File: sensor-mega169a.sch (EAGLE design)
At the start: 55 parts, among them IC3 ATmega169PA, K1 SP6029TOP, M1 NRF24L01P-M, M2 DHT22, Q1 IRLML2502, Q2 IRLML2502, Q3 IRLML6402, U1 MCP1640C, U2 MCP604-I/ST

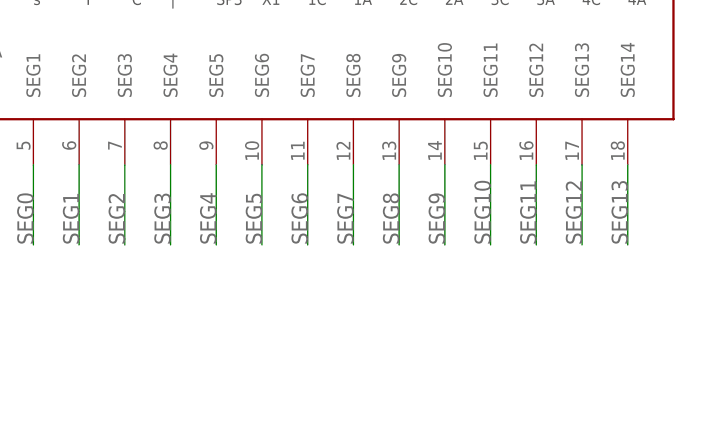
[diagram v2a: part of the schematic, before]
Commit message: cc-by-sa license
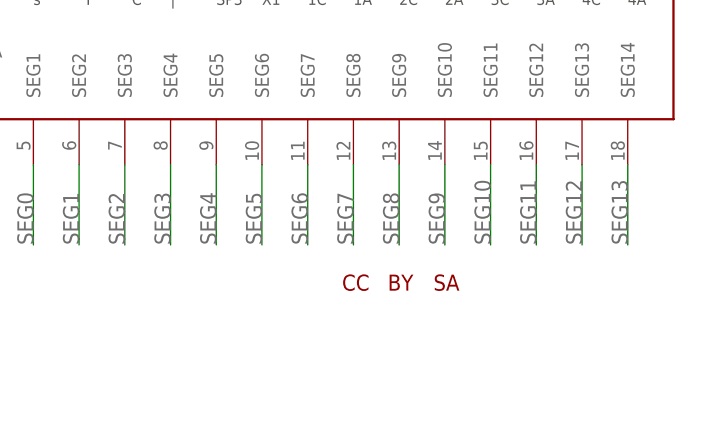
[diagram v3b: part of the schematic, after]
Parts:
- added U$1: CC-TPLACE-HALF, creative-commons:CC-TPLACE-HALF
- added U$3: BY-TPLACE-HS, creative-commons:BY-TPLACE-HS
- added U$4: SA-TPLACE-HALF, creative-commons:SA-TPLACE-HALF

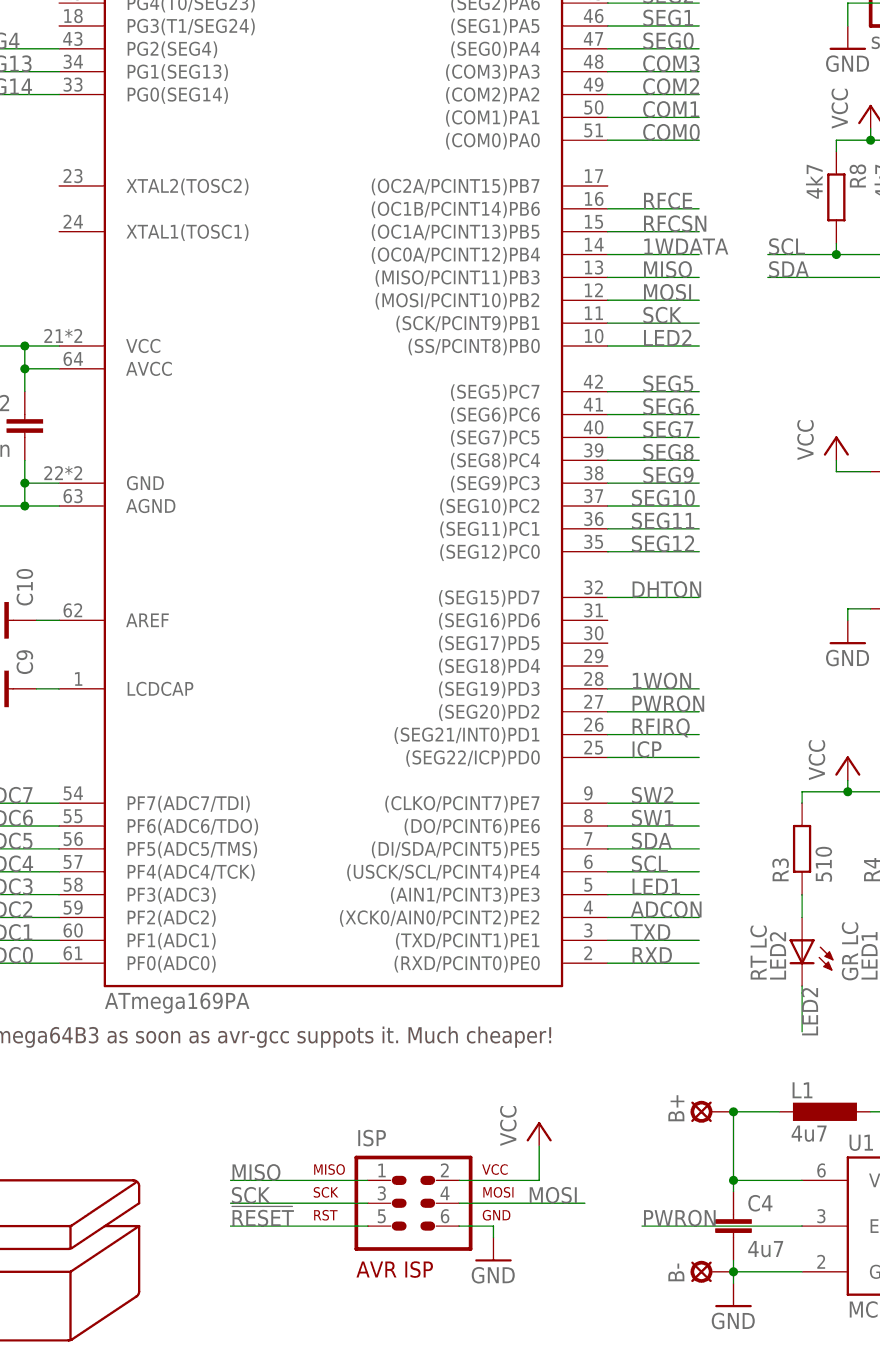
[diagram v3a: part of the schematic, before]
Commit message: added jumper for spi slave extensions on isp header
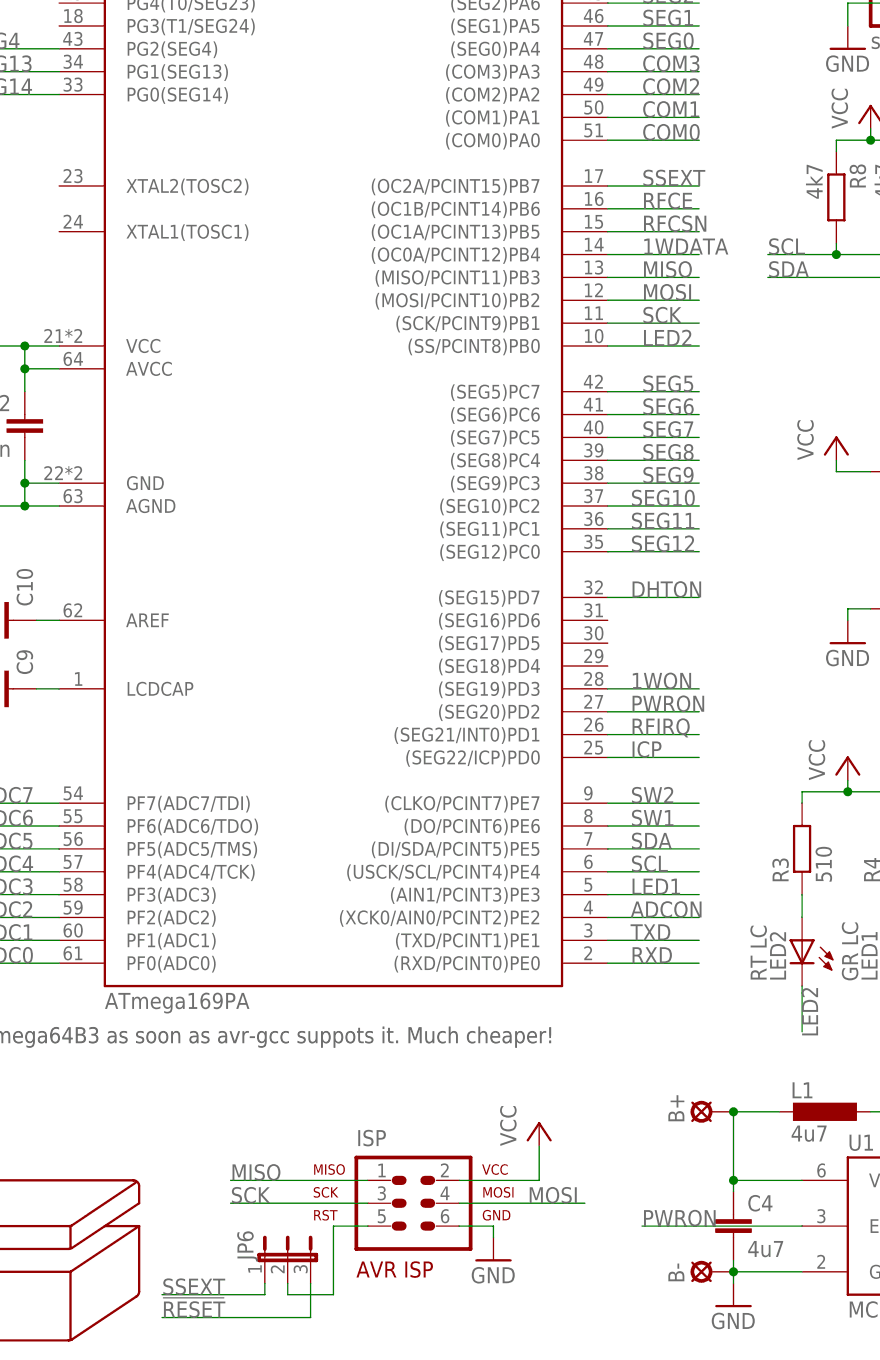
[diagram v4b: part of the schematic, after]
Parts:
- added JP6: (no value), jumper:JP2E
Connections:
- new net N$6: ISP.5, JP6.2
- new net SSEXT: IC3.(OC2A/PCINT15)PB7, JP6.1
- net !RESET: now also JP6.3; no longer ISP.5
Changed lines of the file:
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@@
 <setting verticaltext="up"/>
 </settings>
-<grid distance="0.1" unitdist="inch" unit="mm" style="lines" multiple="1" display="yes" altdistance="0.01" altunitdist="inch" altunit="mm"/>
+<grid distance="1.27" unitdist="mm" unit="mm" style="lines" multiple="1" display="yes" altdistance="635" altunitdist="mic" altunit="mic"/>
 <layers>
-<layer number="1" name="Top" color="4" fill="1" visible="yes" active="no"/>
-<layer number="2" name="Route2" color="1" fill="3" visible="yes" active="no"/>
-<layer number="3" name="Route3" color="4" fill="3" visible="yes" active="no"/>
-<layer number="4" name="Route4" color="1" fill="4" visible="yes" active="no"/>
-<layer number="5" name="Route5" color="4" fill="4" visible="yes" active="no"/>
-<layer number="6" name="Route6" color="1" fill="8" visible="yes" active="no"/>
-<layer number="7" name="Route7" color="4" fill="8" visible="yes" active="no"/>
-<layer number="8" name="Route8" color="1" fill="2" visible="yes" active="no"/>
-<layer number="9" name="Route9" color="4" fill="2" visible="yes" active="no"/>
-<layer number="10" name="Route10" color="1" fill="7" visible="yes" active="no"/>
-<layer number="11" name="Route11" color="4" fill="7" visible="yes" active="no"/>
-<layer number="12" name="Route12" color="1" fill="5" visible="yes" active="no"/>
-<layer number="13" name="Route13" color="4" fill="5" visible="yes" active="no"/>
-<layer number="14" name="Route14" color="1" fill="6" visible="yes" active="no"/>
-<layer number="15" name="Route15" color="4" fill="6" visible="yes" active="no"/>
-<layer number="16" name="Bottom" color="1" fill="1" visible="yes" active="no"/>
-<layer number="17" name="Pads" color="2" fill="1" visible="yes" active="no"/>
-<layer number="18" name="Vias" color="2" fill="1" visible="yes" active="no"/>
-<layer number="19" name="Unrouted" color="6" fill="1" visible="yes" active="no"/>
-<layer number="20" name="Dimension" color="15" fill="1" visible="yes" active="no"/>
-<layer number="21" name="tPlace" color="7" fill="1" visible="yes" active="no"/>
-<layer number="22" name="bPlace" color="7" fill="1" visible="yes" active="no"/>
-<layer number="23" name="tOrigins" color="15" fill="1" visible="yes" active="no"/>
-<layer number="24" name="bOrigins" color="15" fill="1" visible="yes" active="no"/>
-<layer number="25" name="tNames" color="7" fill="1" visible="yes" active="no"/>
-<layer number="26" name="bNames" color="7" fill="1" visible="yes" active="no"/>
-<layer number="27" name="tValues" color="7" fill="1" visible="yes" active="no"/>
-<layer number="28" name="bValues" color="7" fill="1" visible="yes" active="no"/>
+<layer number="1" name="Top" color="4" fill="1" visible="no" active="no"/>
+<layer number="2" name="Route2" color="1" fill="3" visible="no" active="no"/>
+<layer number="3" name="Route3" color="4" fill="3" visible="no" active="no"/>
+<layer number="4" name="Route4" color="1" fill="4" visible="no" active="no"/>
+<layer number="5" name="Route5" color="4" fill="4" visible="no" active="no"/>
+<layer number="6" name="Route6" color="1" fill="8" visible="no" active="no"/>
+<layer number="7" name="Route7" color="4" fill="8" visible="no" active="no"/>
+<layer number="8" name="Route8" color="1" fill="2" visible="no" active="no"/>
+<layer number="9" name="Route9" color="4" fill="2" visible="no" active="no"/>
+<layer number="10" name="Route10" color="1" fill="7" visible="no" active="no"/>
+<layer number="11" name="Route11" color="4" fill="7" visible="no" active="no"/>
+<layer number="12" name="Route12" color="1" fill="5" visible="no" active="no"/>
+<layer number="13" name="Route13" color="4" fill="5" visible="no" active="no"/>
+<layer number="14" name="Route14" color="1" fill="6" visible="no" active="no"/>
+<layer number="15" name="Route15" color="4" fill="6" visible="no" active="no"/>
+<layer number="16" name="Bottom" color="1" fill="1" visible="no" active="no"/>
+<layer number="17" name="Pads" color="2" fill="1" visible="no" active="no"/>
+<layer number="18" name="Vias" color="2" fill="1" visible="no" active="no"/>
+<layer number="19" name="Unrouted" color="6" fill="1" visible="no" active="no"/>
+<layer number="20" name="Dimension" color="15" fill="1" visible="no" active="no"/>
+<layer number="21" name="tPlace" color="7" fill="1" visible="no" active="no"/>
+<layer number="22" name="bPlace" color="7" fill="1" visible="no" active="no"/>
+<layer number="23" name="tOrigins" color="15" fill="1" visible="no" active="no"/>
+<layer number="24" name="bOrigins" color="15" fill="1" visible="no" active="no"/>
+<layer number="25" name="tNames" color="7" fill="1" visible="no" active="no"/>
+<layer number="26" name="bNames" color="7" fill="1" visible="no" active="no"/>
+<layer number="27" name="tValues" color="7" fill="1" visible="no" active="no"/>
+<layer number="28" name="bValues" color="7" fill="1" visible="no" active="no"/>
 <layer number="29" name="tStop" color="7" fill="3" visible="no" active="no"/>
 <layer number="30" name="bStop" color="7" fill="6" visible="no" active="no"/>
@@
 <layer number="35" name="tGlue" color="7" fill="4" visible="no" active="no"/>
 <layer number="36" name="bGlue" color="7" fill="5" visible="no" active="no"/>
-<layer number="37" name="tTest" color="7" fill="1" visible="yes" active="no"/>
-<layer number="38" name="bTest" color="7" fill="1" visible="yes" active="no"/>
+<layer number="37" name="tTest" color="7" fill="1" visible="no" active="no"/>
+<layer number="38" name="bTest" color="7" fill="1" visible="no" active="no"/>
 <layer number="39" name="tKeepout" color="4" fill="11" visible="no" active="no"/>
 <layer number="40" name="bKeepout" color="1" fill="11" visible="no" active="no"/>
@@
 <layer number="44" name="Drills" color="7" fill="1" visible="no" active="no"/>
 <layer number="45" name="Holes" color="7" fill="1" visible="no" active="no"/>
-<layer number="46" name="Milling" color="3" fill="1" visible="yes" active="no"/>
-<layer number="47" name="Measures" color="7" fill="1" visible="yes" active="no"/>
-<layer number="48" name="Document" color="7" fill="1" visible="yes" active="no"/>
-<layer number="49" name="Reference" color="7" fill="1" visible="yes" active="no"/>
-<layer number="50" name="dxf" color="7" fill="1" visible="yes" active="no"/>
-<layer number="51" name="tDocu" color="7" fill="1" visible="yes" active="no"/>
-<layer number="52" name="bDocu" color="7" fill="1" visible="yes" active="no"/>
-<layer number="53" name="tGND_GNDA" color="7" fill="9" visible="yes" active="no"/>
-<layer number="54" name="bGND_GNDA" color="1" fill="9" visible="yes" active="no"/>
-<layer number="56" name="wert" color="7" fill="1" visible="yes" active="no"/>
+<layer number="46" name="Milling" color="3" fill="1" visible="no" active="no"/>
+<layer number="47" name="Measures" color="7" fill="1" visible="no" active="no"/>
+<layer number="48" name="Document" color="7" fill="1" visible="no" active="no"/>
+<layer number="49" name="Reference" color="7" fill="1" visible="no" active="no"/>
+<layer number="50" name="dxf" color="7" fill="1" visible="no" active="no"/>
+<layer number="51" name="tDocu" color="7" fill="1" visible="no" active="no"/>
+<layer number="52" name="bDocu" color="7" fill="1" visible="no" active="no"/>
+<layer number="53" name="tGND_GNDA" color="7" fill="9" visible="no" active="no"/>
+<layer number="54" name="bGND_GNDA" color="1" fill="9" visible="no" active="no"/>
+<layer number="56" name="wert" color="7" fill="1" visible="no" active="no"/>
 <layer number="91" name="Nets" color="2" fill="1" visible="yes" active="yes"/>
 <layer number="92" name="Busses" color="1" fill="1" visible="yes" active="yes"/>
@@
 <part name="U$3" library="creative-commons" deviceset="BY" device="-TPLACE-HS" value="BY-TPLACE-HS"/>
 <part name="U$4" library="creative-commons" deviceset="SA" device="-TPLACE-HALF" value="SA-TPLACE-HALF"/>
+<part name="JP6" library="jumper" deviceset="JP2E" device=""/>
 </parts>
 <sheets>
@@
 <instance part="U$3" gate="G$1" x="223.52" y="20.32"/>
 <instance part="U$4" gate="G$1" x="228.6" y="20.32"/>
+<instance part="JP6" gate="1" x="49.53" y="13.97"/>
 </instances>
 <busses>
@@
 </segment>
 <segment>
-<pinref part="ISP" gate="G$1" pin="5"/>
-<wire x1="58.42" y1="17.78" x2="43.18" y2="17.78" width="0.1524" layer="91"/>
-<label x="43.18" y="17.78" size="1.778" layer="95"/>
+<label x="35.56" y="7.62" size="1.778" layer="95"/>
+<wire x1="35.56" y1="7.62" x2="52.07" y2="7.62" width="0.1524" layer="91"/>
+<pinref part="JP6" gate="1" pin="3"/>
+<wire x1="52.07" y1="7.62" x2="52.07" y2="11.43" width="0.1524" layer="91"/>
 </segment>
 </net>
@@
 </segment>
 </net>
+<net name="SSEXT" class="0">
+<segment>
+<pinref part="IC3" gate="G$1" pin="(OC2A/PCINT15)PB7"/>
+<wire x1="85.09" y1="133.35" x2="95.25" y2="133.35" width="0.1524" layer="91"/>
+<label x="88.9" y="133.35" size="1.778" layer="95"/>
+</segment>
+<segment>
+<wire x1="46.99" y1="10.16" x2="35.56" y2="10.16" width="0.1524" layer="91"/>
+<label x="35.56" y="10.16" size="1.778" layer="95"/>
+<pinref part="JP6" gate="1" pin="1"/>
+<wire x1="46.99" y1="11.43" x2="46.99" y2="10.16" width="0.1524" layer="91"/>
+</segment>
+</net>
+<net name="N$6" class="0">
+<segment>
+<pinref part="JP6" gate="1" pin="2"/>
+<wire x1="49.53" y1="11.43" x2="49.53" y2="10.16" width="0.1524" layer="91"/>
+<wire x1="49.53" y1="10.16" x2="54.61" y2="10.16" width="0.1524" layer="91"/>
+<wire x1="54.61" y1="10.16" x2="54.61" y2="17.78" width="0.1524" layer="91"/>
+<pinref part="ISP" gate="G$1" pin="5"/>
+<wire x1="54.61" y1="17.78" x2="58.42" y2="17.78" width="0.1524" layer="91"/>
+</segment>
+</net>
